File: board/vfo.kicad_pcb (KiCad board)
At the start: 2 copper layers, 19 x 100 mm, 36 parts, among them J1 CVIN, J2 SAW, J3 TRI, J4 Conn_02x05_Odd_Even, J5 Conn_01x06, U1 TL072, U2 AS3340

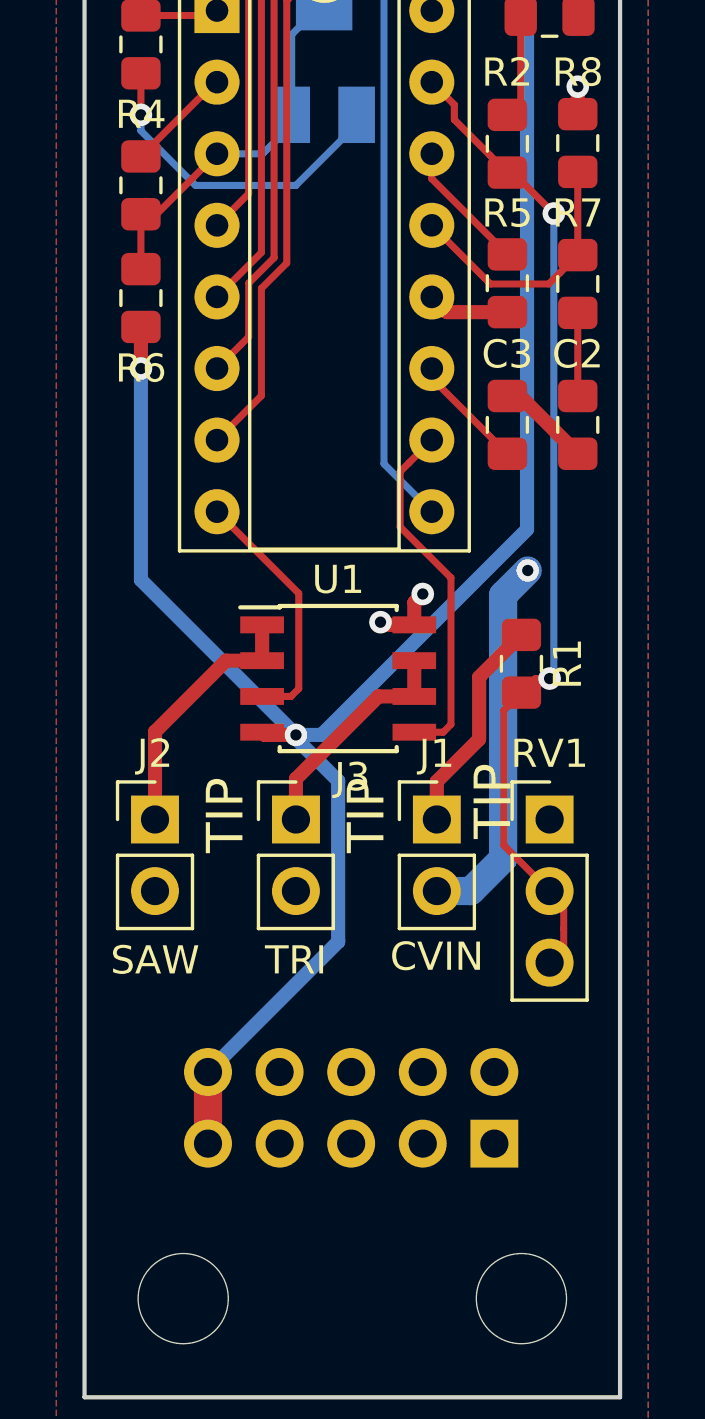
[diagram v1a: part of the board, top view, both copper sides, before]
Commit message: Add missing 100K resistor
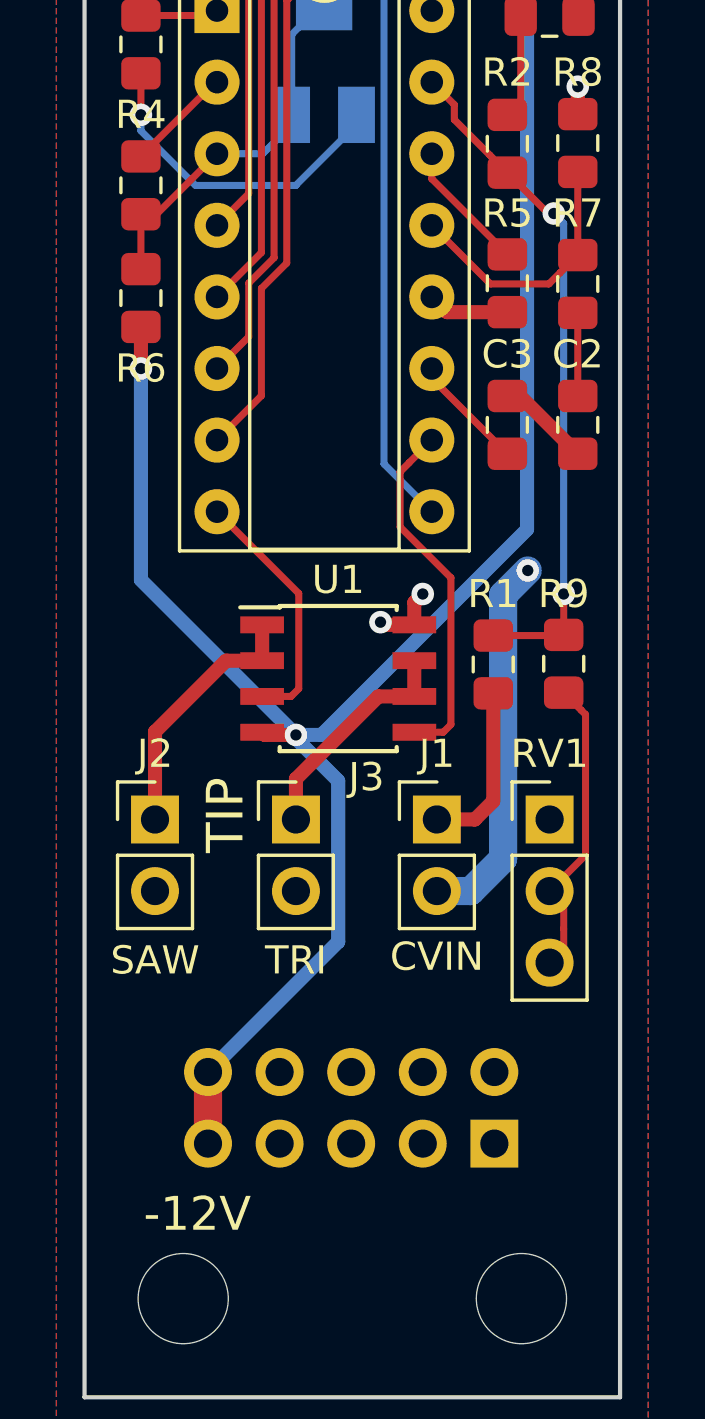
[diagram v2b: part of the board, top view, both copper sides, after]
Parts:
- added R9: 100K, Resistor_SMD:R_0805_2012Metric_Pad1.15x1.40mm_HandSolder, F.Cu at (136.0, 146.0)
- R2: value 470K -> 470R
- R6: value 820R -> 620R
- moved R1 1.00 mm to (133.5, 146.0), turned to 90 degrees
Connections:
- RV1 pad 2: /VFCI -> Net-(R9-Pad1)
- RV1 pad 3: /VFCI -> Net-(R9-Pad1)
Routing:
- net /VFCI: track 34.9 -> 24.2 mm
- net Net-(R9-Pad1): track 0.00 -> 10.4 mm
- net /CVIN: track 7.79 -> 6.09 mm

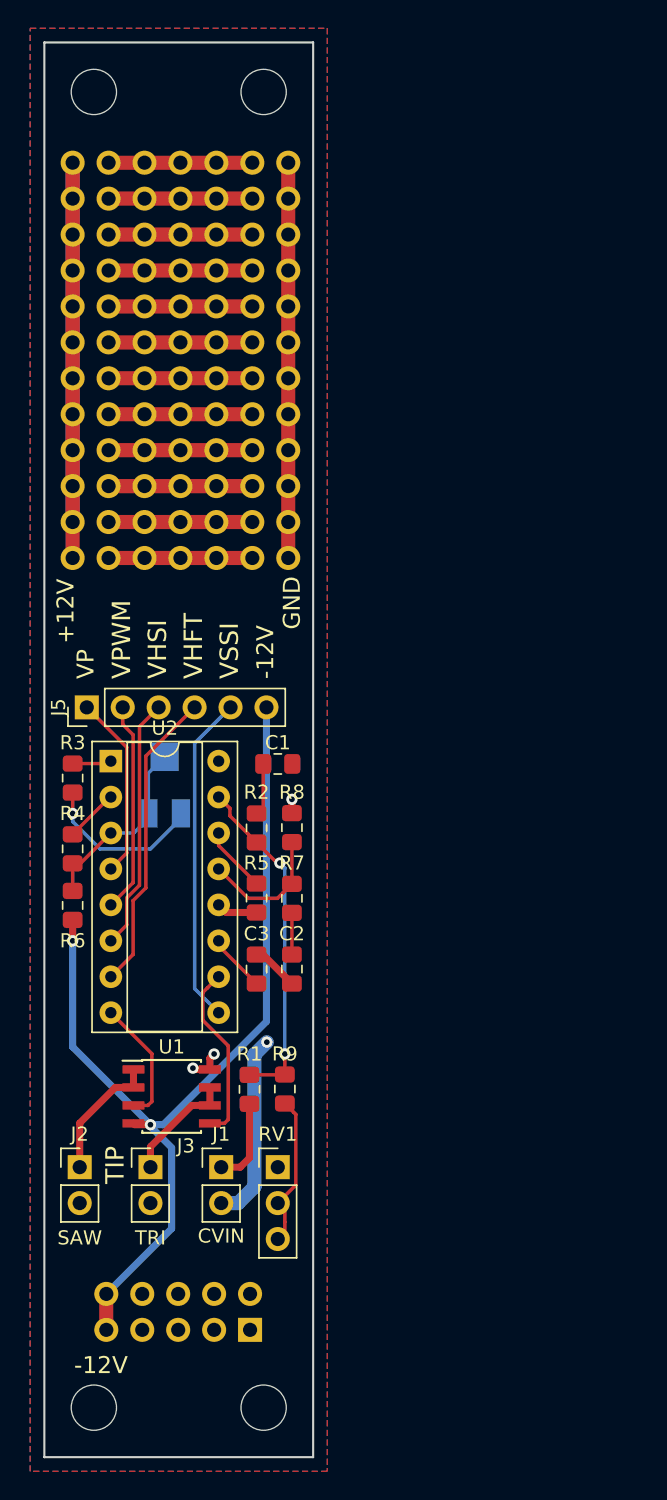
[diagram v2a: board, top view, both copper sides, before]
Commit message: Break into two boards
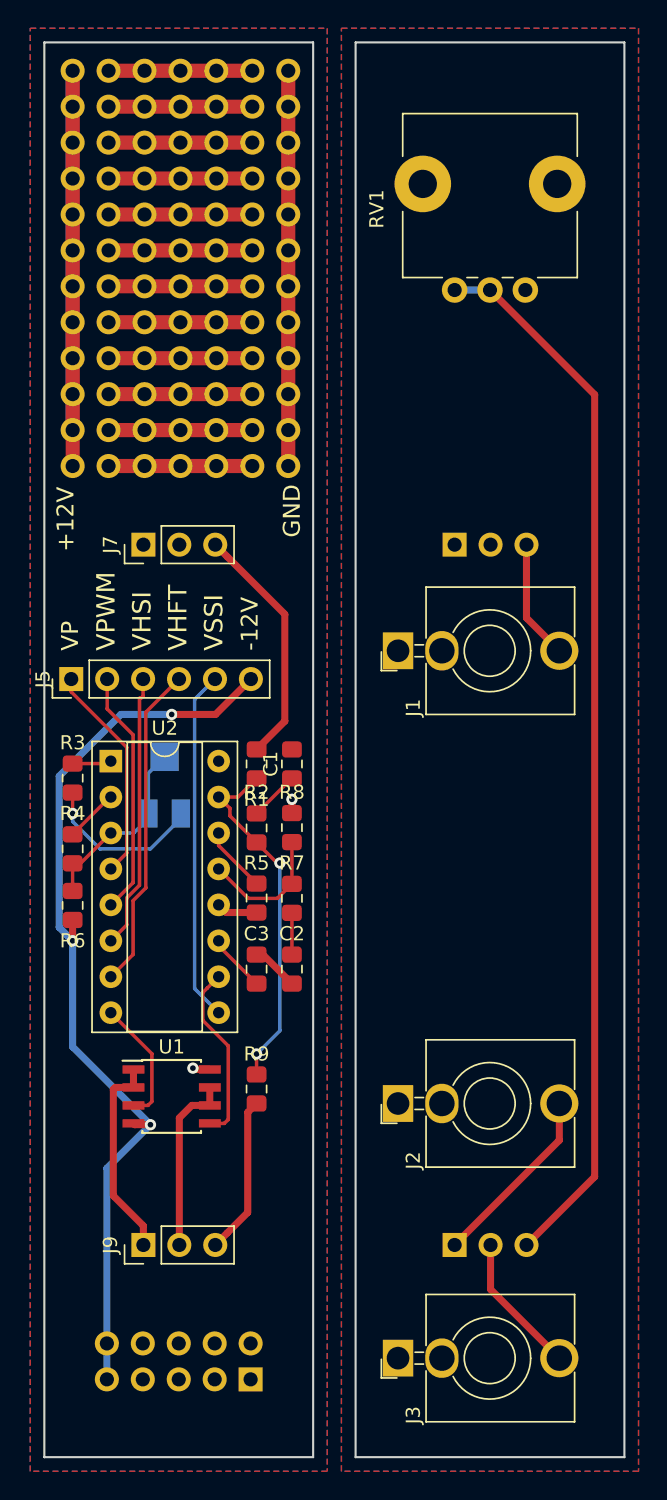
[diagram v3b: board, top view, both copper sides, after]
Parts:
- removed the REF** at (121.0, 108.4)
- removed the REF** at (121.0, 85.6)
- removed the REF** at (121.0, 83.0)
- removed the REF** at (134.5, 75.5)
- removed the REF** at (134.5, 168.5)
- removed the REF** at (122.5, 75.5)
- removed the REF** at (122.5, 168.5)
- removed the REF** at (121.0, 80.5)
- removed the REF** at (121.0, 105.9)
- removed the REF** at (121.0, 103.4)
- removed the REF** at (121.0, 100.8)
- removed the REF** at (121.0, 98.3)
- removed the REF** at (121.0, 95.7)
- removed the REF** at (121.0, 93.2)
- removed the REF** at (121.0, 90.7)
- removed the REF** at (121.0, 88.1)
- added J6: Daughter_top, Connector_PinSocket_2.54mm:PinSocket_1x03_P2.54mm_Vertical, B.Cu at (148.0, 107.5)
- added J7: Mother_top, Connector_PinHeader_2.54mm:PinHeader_1x03_P2.54mm_Vertical, F.Cu at (126.0, 107.5)
- added J8: Daughter_bottom, Connector_PinSocket_2.54mm:PinSocket_1x03_P2.54mm_Vertical, B.Cu at (148.0, 157.0)
- added J9: Mother_bottom, Connector_PinHeader_2.54mm:PinHeader_1x03_P2.54mm_Vertical, F.Cu at (126.0, 157.0)
- added REF**: Breadboard_1x07_P2.54mm, Staticfree:Breadboard_1x07_P2.54mm, F.Cu at (121.0, 101.9)
- added REF**: Breadboard_1x07_P2.54mm, Staticfree:Breadboard_1x07_P2.54mm, F.Cu at (121.0, 79.1)
- added REF**: Breadboard_1x07_P2.54mm, Staticfree:Breadboard_1x07_P2.54mm, F.Cu at (121.0, 76.5)
- added REF**: Breadboard_1x07_P2.54mm, Staticfree:Breadboard_1x07_P2.54mm, F.Cu at (121.0, 74.0)
- added REF**: Breadboard_1x07_P2.54mm, Staticfree:Breadboard_1x07_P2.54mm, F.Cu at (121.0, 99.4)
- added REF**: Breadboard_1x07_P2.54mm, Staticfree:Breadboard_1x07_P2.54mm, F.Cu at (121.0, 96.9)
- added REF**: Breadboard_1x07_P2.54mm, Staticfree:Breadboard_1x07_P2.54mm, F.Cu at (121.0, 94.3)
- added REF**: Breadboard_1x07_P2.54mm, Staticfree:Breadboard_1x07_P2.54mm, F.Cu at (121.0, 91.8)
- added REF**: Breadboard_1x07_P2.54mm, Staticfree:Breadboard_1x07_P2.54mm, F.Cu at (121.0, 89.2)
- added REF**: Breadboard_1x07_P2.54mm, Staticfree:Breadboard_1x07_P2.54mm, F.Cu at (121.0, 86.7)
- added REF**: Breadboard_1x07_P2.54mm, Staticfree:Breadboard_1x07_P2.54mm, F.Cu at (121.0, 84.2)
- added REF**: Breadboard_1x07_P2.54mm, Staticfree:Breadboard_1x07_P2.54mm, F.Cu at (121.0, 81.6)
- J1, J2, J3: footprint Connector_PinHeader_2.54mm:PinHeader_1x02_P2.54mm_Vertical -> Connector_Audio:Jack_3.5mm_QingPu_WQP-PJ398SM_Vertical_CircularHoles
- RV1: footprint Connector_PinHeader_2.54mm:PinHeader_1x03_P2.54mm_Vertical -> Potentiometer_THT:Potentiometer_Alps_RK09L_Single_Vertical
- moved RV1 64.4 mm to (153.0, 89.5), turned to 90 degrees
- moved J1 38.6 mm to (144.0, 115.0), turned to 90 degrees
- moved R1 23.0 mm to (134.0, 123.0), turned to 270 degrees
- moved J2 22.9 mm to (144.0, 147.0), turned to 90 degrees
- moved J3 22.1 mm to (144.0, 165.0), turned to 90 degrees
- moved J4 3.50 mm to (133.6, 166.5)
- moved J5 2.28 mm to (120.9, 117.0)
- moved R9 2.00 mm to (134.0, 146.0)
- moved C1 1.00 mm to (136.5, 123.0), turned to 270 degrees
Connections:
- R1 pad 1: /CVIN -> /CV_IN
- R9 pad 1: Net-(R9-Pad1) -> /TUNE_POT
- RV1 pad 1: +12V -> /D_12V
- RV1 pad 2: Net-(R9-Pad1) -> /D_TUNE_POT
- RV1 pad 3: Net-(R9-Pad1) -> /D_TUNE_POT
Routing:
- net /D_TUNE_POT: track 0.00 -> 75.1 mm
- net /CV_IN: track 0.00 -> 17.3 mm
- net GND: track 47.6 -> 34.2 mm, vias 1 -> 0
- net /D_SAW_OUT: track 0.00 -> 13.1 mm
- net /TUNE_POT: track 0.00 -> 11.2 mm
- net Net-(R9-Pad1): track 10.4 -> 0.00 mm
- net /D_TRI_OUT: track 0.00 -> 10.0 mm
- net /D_CV_IN: track 0.00 -> 8.46 mm
- net /CVIN: track 6.09 -> 0.00 mm
- net /SAW_OUT: track 9.23 -> 14.6 mm
- net /TRI_OUT: track 8.12 -> 12.8 mm
- net -12V: track 68.5 -> 66.0 mm, vias 2 -> 3
- net /VPWM: track 14.9 -> 17.4 mm
- net /VP: track 13.1 -> 15.5 mm
- net /VHSI: track 17.9 -> 19.5 mm
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- added copper zone on B.Cu, net /D_12V
- added copper zone on F.Cu, net /D_GND
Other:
- board size 19 x 100 mm -> 41 x 100 mm
- board text removed: "TIP"

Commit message: Add labels
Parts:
- added REF**: OSHW-Logo2_7.3x6mm_SilkScreen, Symbol:OSHW-Logo2_7.3x6mm_SilkScreen, B.Cu at (128.5, 112.5)
- added REF**: OSHW-Logo2_7.3x6mm_SilkScreen, Symbol:OSHW-Logo2_7.3x6mm_SilkScreen, B.Cu at (150.5, 136.5)
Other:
- board text added: "Fine tune"
- board text added: "VCO v1.1.0 2018 Steve Pomeroy staticfree.info"

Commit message: Add protection diodes
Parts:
- added D1: DIODE, Diode_SMD:D_0805_2012Metric_Pad1.15x1.40mm_HandSolder, F.Cu at (134.0, 160.0)
- added D2: DIODE, Diode_SMD:D_0805_2012Metric_Pad1.15x1.40mm_HandSolder, F.Cu at (123.0, 160.0)
- added REF**: MountingHole_2.7mm_M2.5_ISO7380, MountingHole:MountingHole_2.7mm_M2.5_ISO7380, F.Cu at (121.5, 107.5)
- added REF**: MountingHole_2.7mm_M2.5_ISO7380, MountingHole:MountingHole_2.7mm_M2.5_ISO7380, F.Cu at (144.0, 107.5)
- added REF**: MountingHole_2.7mm_M2.5_ISO7380, MountingHole:MountingHole_2.7mm_M2.5_ISO7380, F.Cu at (135.5, 154.5)
- added REF**: MountingHole_2.7mm_M2.5_ISO7380, MountingHole:MountingHole_2.7mm_M2.5_ISO7380, F.Cu at (157.5, 154.5)
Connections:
- J4 pad 1: +12V -> /12V_IN
- J4 pad 10: -12V -> /-12V_IN
- J4 pad 2: +12V -> /12V_IN
- J4 pad 9: -12V -> /-12V_IN
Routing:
- net -12V: track 66.0 -> 57.8 mm, vias 3 -> 4
- net /-12V_IN: track 0.00 -> 5.65 mm
- net /12V_IN: track 0.00 -> 5.62 mm
- net +12V: track 55.6 -> 60.1 mm, vias 2 -> 5
